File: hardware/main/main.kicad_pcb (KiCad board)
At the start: 4 copper layers, 59.7 x 109.5 mm, 218 parts, among them J101 ST_LINK, J102 USART, J301 Overvoltage_protection, J302 Rad_sensor, J303 Mos_temp, J304 Diode_temp, J601 Supplies, J801 RJ45_Shielded, J802 RJ45_Shielded, Q401 BSC093N15NS5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

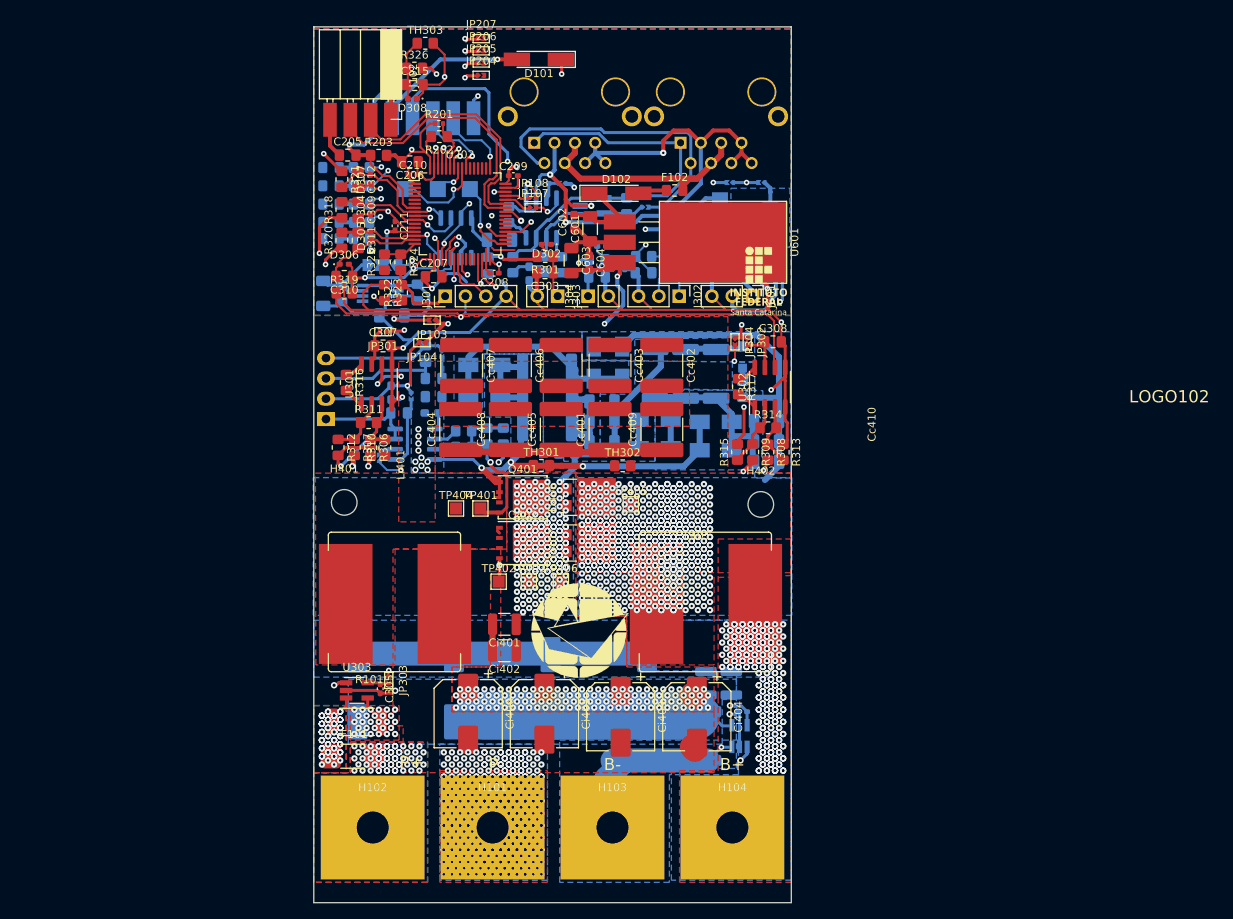
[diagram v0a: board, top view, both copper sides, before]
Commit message: Layout: Designing thermal dissipation and optimizing control
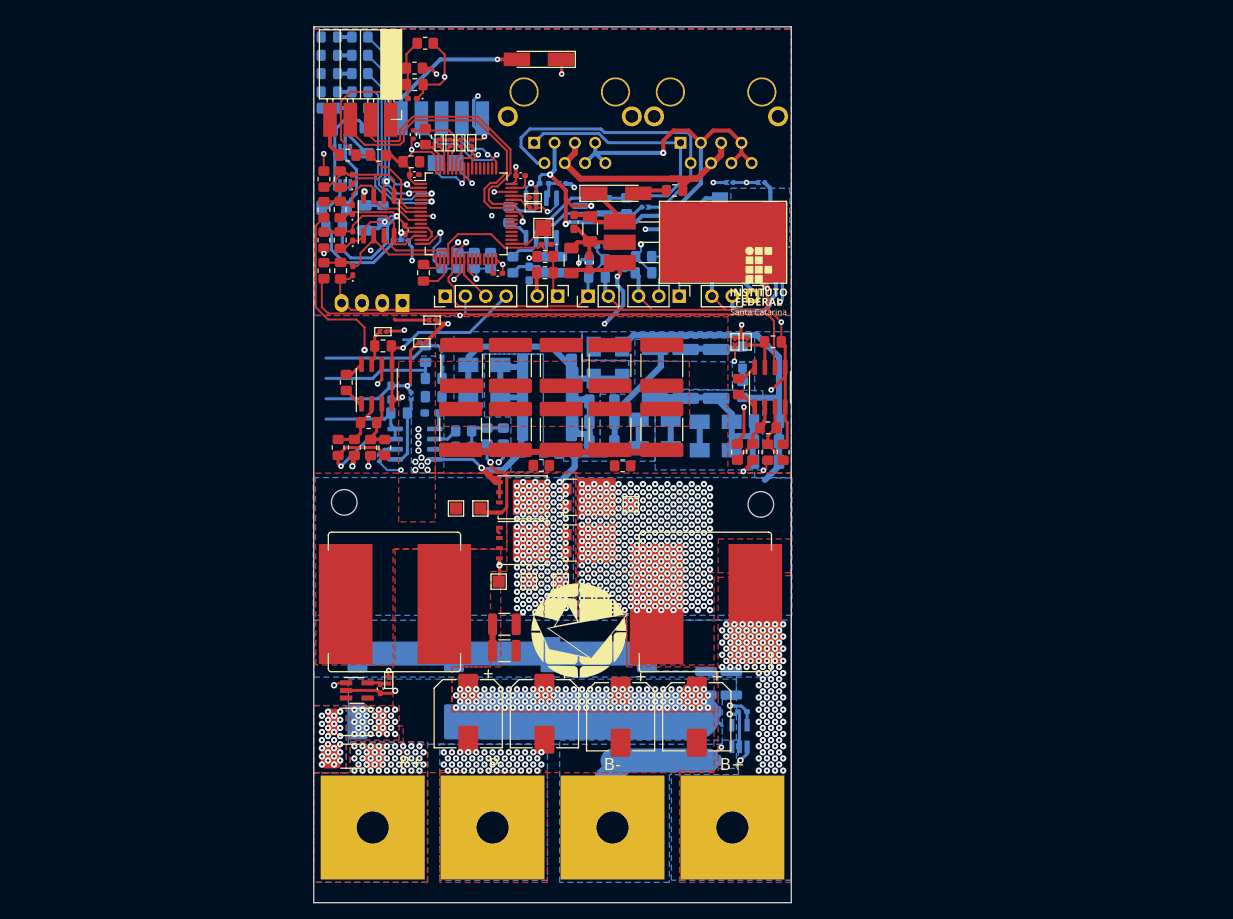
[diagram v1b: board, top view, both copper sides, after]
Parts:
- added HS401: HS10334, Zenite:HS10334 60mmx17mm, B.Cu at (78.7, 156.0)
- D201: value CAN_TX_LED -> CAN_BUSY
- D202: value CAN_RX_LED -> STATUS_LED
- JP203: footprint Jumper:SolderJumper-3_P2.0mm_Open_TrianglePad1.0x1.5mm -> Zenite:SolderJumper-3_P0.5mm_Open_TrianglePad0.8x0.5mm
- R322, R323, R324, R325: moved to B.Cu
- TP203, U305: moved to F.Cu
- moved C202 22.4 mm to (22.3, 95.4), turned to 180 degrees
- moved C201 22.1 mm to (25.4, 96.8), turned to 90 degrees
- moved PS501 17.4 mm to (29.9, 117.1), turned to 90 degrees
- moved C313 17.1 mm to (25.1, 106.4), turned to -90 degrees
- moved U201 16.4 mm to (22.4, 100.1), turned to -90 degrees
- moved D201 16.3 mm to (20.7, 90.7)
- moved D202 16.3 mm to (20.7, 88.4)
- moved D203 16.3 mm to (20.7, 86.1)
- moved D204 16.3 mm to (20.7, 83.8)
- moved D205 16.3 mm to (20.7, 92.7)
- moved R204 16.3 mm to (24.6, 90.7)
- moved R205 16.3 mm to (24.6, 88.4)
- moved R206 16.3 mm to (24.6, 86.1)
- moved R207 16.3 mm to (24.6, 83.8)
- moved R208 16.3 mm to (24.6, 92.7)
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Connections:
- R204 pad 1: Net-(R204-Pad1) -> /STM32/CAN_BUSY
- R205 pad 1: Net-(R205-Pad1) -> /STM32/STATUS_LED
- R206 pad 1: Net-(R206-Pad1) -> /STM32/LED_1
- R207 pad 1: Net-(R207-Pad1) -> /STM32/LED_0
- U202 pad 2: unconnected-(U202-Pad2) -> /STM32/LED_0
- U202 pad 29: Net-(R204-Pad1) -> unconnected-(U202-Pad29)
- U202 pad 3: unconnected-(U202-Pad3) -> /STM32/LED_1
- U202 pad 30: Net-(R205-Pad1) -> unconnected-(U202-Pad30)
- U202 pad 35: Net-(R206-Pad1) -> unconnected-(U202-Pad35)
- U202 pad 36: Net-(R207-Pad1) -> unconnected-(U202-Pad36)
- U202 pad 4: unconnected-(U202-Pad4) -> /STM32/STATUS_LED
- U202 pad 5: unconnected-(U202-Pad5) -> /STM32/CAN_BUSY
- U305 pad 2: /Analog/V_temp_diode -> /Analog/V_bat_adc+
- U305 pad 3: /Analog/V_bat_adc+ -> /Analog/V_temp_mos
- U305 pad 6: /Analog/V_panel_adc+ -> /Analog/V_temp_diode
- U305 pad 7: /Analog/V_temp_mos -> /Analog/V_panel_adc+
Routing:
- net Net-(R321-Pad1): track 27.1 -> 131.8 mm
- net Net-(R207-Pad1): track 34.2 -> 0.00 mm, vias 2 -> 0
- net Net-(R206-Pad1): track 27.2 -> 0.00 mm, vias 2 -> 0
- net Net-(R205-Pad1): track 26.4 -> 0.00 mm, vias 2 -> 0
- net /Cuk/S: track 84.8 -> 58.7 mm, vias 13 -> 11
- net /STM32/STATUS_LED: track 0.00 -> 24.0 mm, vias 0 -> 1
- net /STM32/LED_0: track 0.00 -> 23.1 mm, vias 0 -> 1
- net Net-(R204-Pad1): track 23.1 -> 0.00 mm, vias 2 -> 0
- net /STM32/CAN_BUSY: track 0.00 -> 22.4 mm, vias 0 -> 1
- net /STM32/LED_1: track 0.00 -> 22.4 mm, vias 0 -> 1
- net Net-(JP207-Pad1): track 21.6 -> 2.94 mm, vias 2 -> 0
- net Net-(JP206-Pad1): track 17.4 -> 2.83 mm, vias 2 -> 0
- net GND: track 524.5 -> 539.0 mm, vias 19 -> 20
- net /Analog/Vbat_comp_EXT: track 19.1 -> 5.92 mm, vias 2 -> 1
- net Net-(JP205-Pad1): track 15.3 -> 2.98 mm, vias 2 -> 0
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
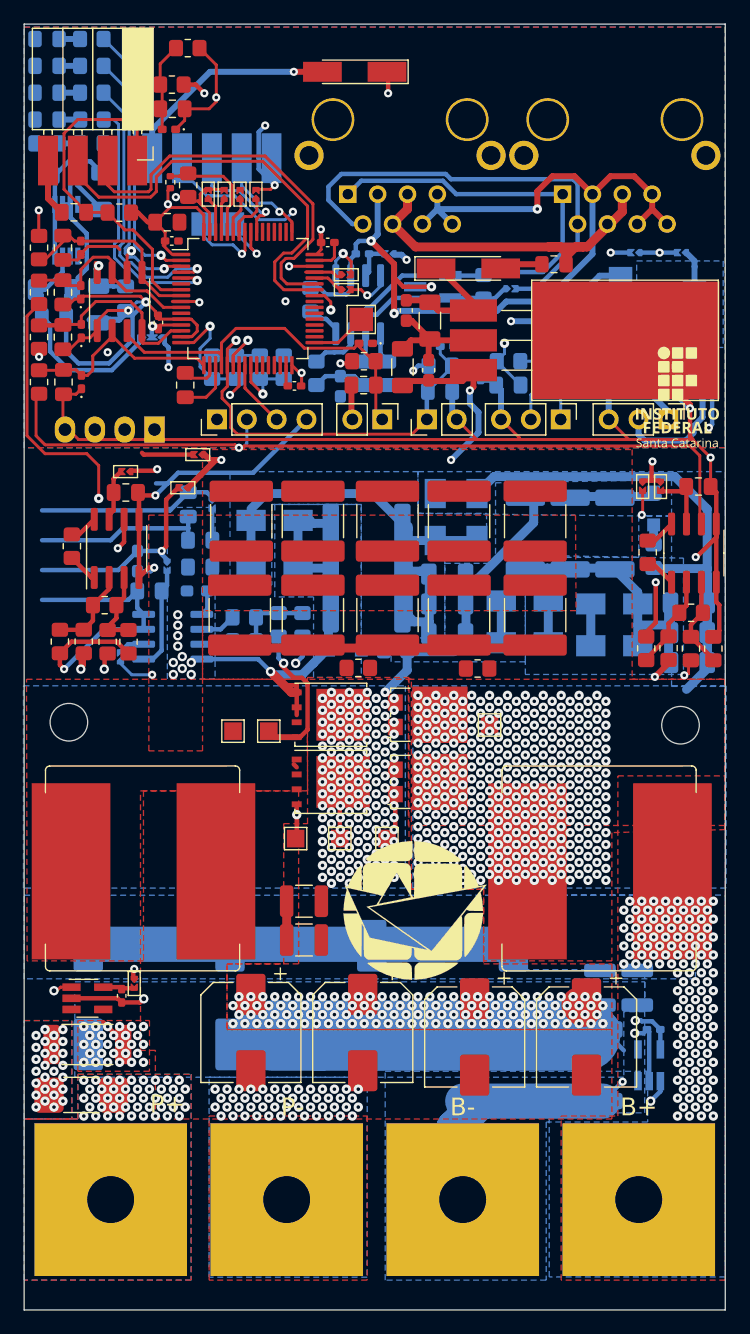
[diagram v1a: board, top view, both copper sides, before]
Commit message: Layout: Connect all unconected nets, and fix all DRC errors
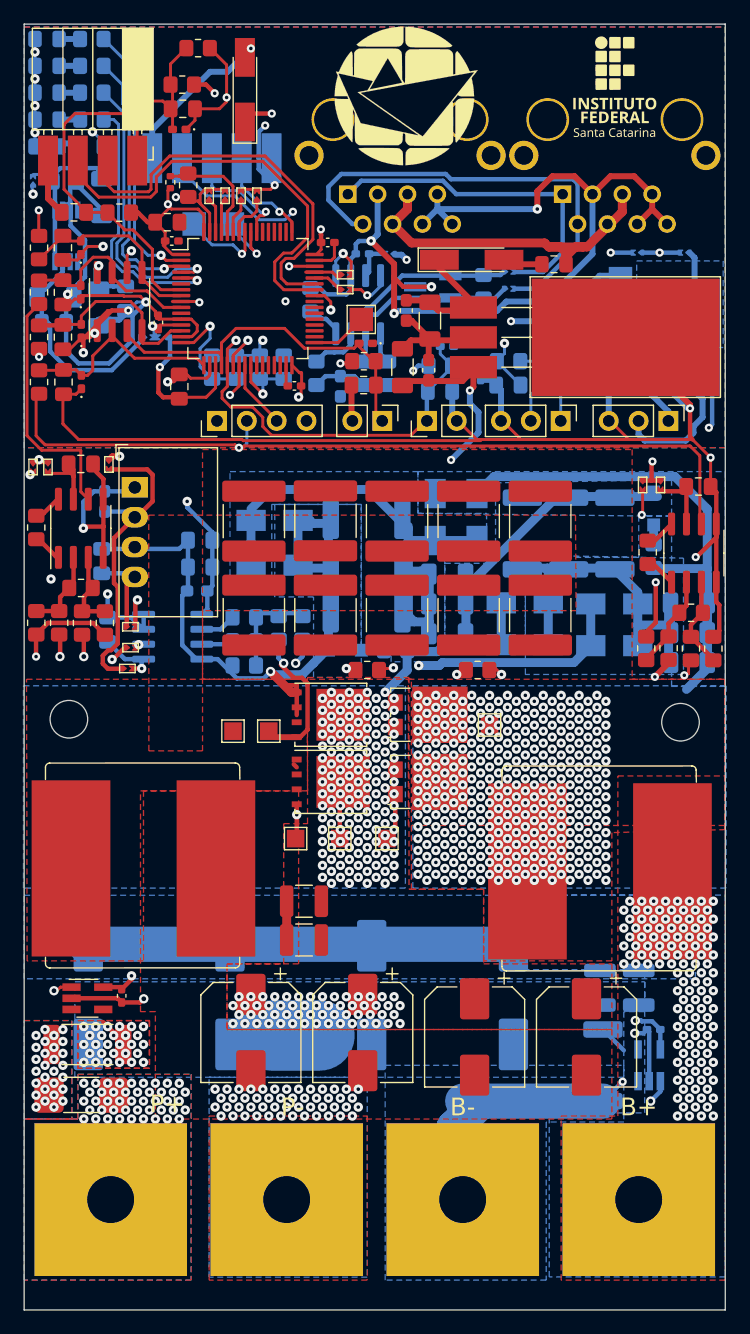
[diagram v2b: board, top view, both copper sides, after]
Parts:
- added R401: 10kR 0805, Resistor_SMD:R_0805_2012Metric_Pad1.20x1.40mm_HandSolder, B.Cu at (37.5, 137.2)
- JP101, JP102, JP104, JP105, JP107, JP108, JP109, JP110, JP201, JP204, JP205, JP206, JP207, JP301, JP302, JP303, JP304: footprint Zenite:SolderJumper-2_P0.5mm_Open_TrianglePad0.5x0.5mm -> Zenite:SolderJumper-2_P0.5mm_Open_TrianglePad0.8x0.5mm
- JP103: footprint Zenite:SolderJumper-2_P0.5mm_Open_TrianglePad0.5x0.5mm -> Zenite:SolderJumper-2_P0.5mm_Open_TrianglePad0.8x0.5mm; moved to B.Cu
- JP106, JP501, JP502: footprint Zenite:SolderJumper-2_P0.5mm_Open_TrianglePad0.5x0.5mm -> Zenite:SolderJumper-2_P0.5mm_Open_TrianglePad0.8x0.5mm; moved to F.Cu
- PS501: moved to F.Cu
- moved LOGO101 69.3 mm to (51.3, 88.6)
- moved JP303 44.2 mm to (19.6, 120.9)
- moved JP103 27.7 mm to (19.6, 95.3), turned to 90 degrees
- moved LOGO102 26.9 mm to (69.1, 87.9)
- moved JP501 12.2 mm to (28.4, 133.9), turned to 0 degrees
- moved D101 9.47 mm to (37.6, 88.1), turned to 90 degrees
- moved JP502 9.12 mm to (28.2, 137.4), turned to 0 degrees
- moved C502 8.81 mm to (25.4, 128.3), turned to 90 degrees
- moved JP301 6.61 mm to (20.8, 120.9), turned to -90 degrees
- moved JP104 6.45 mm to (26.0, 120.7), turned to -90 degrees
- moved C501 5.80 mm to (25.7, 123.2), turned to -90 degrees
- moved PS501 5.20 mm to (28.2, 122.0), turned to 0 degrees
- moved C503 4.85 mm to (25.9, 134.1), turned to 90 degrees
- moved C307 4.54 mm to (23.6, 120.0)
- moved U301 3.50 mm to (23.6, 125.5)
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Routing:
- net GND: track 539.0 -> 609.3 mm, vias 20 -> 32
- net /Analog/3V3_IPanel: track 2.73 -> 51.2 mm, vias 0 -> 2
- net +5V: track 86.7 -> 124.2 mm, vias 5 -> 6
- net /Cuk/S: track 58.7 -> 91.6 mm, vias 11 -> 2
- net /Cuk/A: track 84.4 -> 54.2 mm, vias 302 -> 234
- net /Cuk/C: track 76.0 -> 50.6 mm
- net /3V3_Analog: track 182.8 -> 160.3 mm
- net /Analog/V_temp_diode: track 51.2 -> 73.6 mm, vias 2 -> 3
- net /STM32/Bat_OverV_Out: track 16.6 -> 37.7 mm
- net /Analog/V_temp_mos: track 32.9 -> 53.0 mm, vias 0 -> 1
- net /Cuk/driver/+15V_isolated: track 9.34 -> 24.0 mm, vias 0 -> 2
- net /STM32/3V3_MCU: track 92.6 -> 106.3 mm
- net /3V3_STM: track 34.2 -> 44.5 mm
- net Net-(C502-Pad1): track 15.4 -> 6.06 mm
- net Net-(R318-Pad1): track 29.2 -> 21.1 mm, vias 2 -> 0
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- added copper zone on In1.Cu, net /B+
- added copper zone on In2.Cu, net /B+
- added copper zone on In1.Cu, net /Cuk/A
- added copper zone on In2.Cu, net /Cuk/A
- added copper zone on In1.Cu, net /Cuk/C
- added copper zone on In2.Cu, net /Cuk/C
- added copper zone on In1.Cu, net /P+
- added copper zone on In2.Cu, net /P+
- added copper zone on In1.Cu, net GND
- added copper zone on In2.Cu, net GND

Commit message: Layout: Create Copper zone under NTC temperature sensor for a better thermal coupling
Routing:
- net GND: track 609.3 -> 608.7 mm
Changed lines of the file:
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@@
   (segment (start 54.9656 108.3056) (end 55.621 108.961) (width 0.508) (layer "In1.Cu") (net 1))
   (segment (start 54.727 117.055) (end 54.771 117.055) (width 0.254) (layer "In2.Cu") (net 1))
-  (segment (start 48.702 118.806) (end 48.702 135.956) (width 0.254) (layer "In2.Cu") (net 1))
+  (segment (start 46.741 116.845) (end 48.702 118.806) (width 0.254) (layer "In2.Cu") (net 1))
   (segment (start 58.201 136.687) (end 55.287052 136.687) (width 0.254) (layer "In2.Cu") (net 1))
   (segment (start 53.535 134.934948) (end 53.535 118.247) (width 0.254) (layer "In2.Cu") (net 1))
-  (segment (start 47.244 137.414) (end 46.228 137.414) (width 0.254) (layer "In2.Cu") (net 1))
+  (segment (start 48.702 118.806) (end 48.702 134.432) (width 0.254) (layer "In2.Cu") (net 1))
+  (segment (start 46.228 136.906) (end 46.228 137.414) (width 0.254) (layer "In2.Cu") (net 1))
   (segment (start 53.535 118.247) (end 54.727 117.055) (width 0.254) (layer "In2.Cu") (net 1))
-  (segment (start 48.702 135.956) (end 47.244 137.414) (width 0.254) (layer "In2.Cu") (net 1))
   (segment (start 19.812 135.412144) (end 21.082 134.142144) (width 0.381) (layer "In2.Cu") (net 1))
   (segment (start 19.812 136.398) (end 19.812 135.412144) (width 0.381) (layer "In2.Cu") (net 1))
+  (segment (start 48.702 134.432) (end 46.228 136.906) (width 0.254) (layer "In2.Cu") (net 1))
   (segment (start 59.436 137.922) (end 58.201 136.687) (width 0.254) (layer "In2.Cu") (net 1))
   (segment (start 21.082 134.142144) (end 21.082 129.794) (width 0.381) (layer "In2.Cu") (net 1))
   (segment (start 54.771 117.055) (end 55.621 116.205) (width 0.254) (layer "In2.Cu") (net 1))
   (segment (start 55.287052 136.687) (end 53.535 134.934948) (width 0.254) (layer "In2.Cu") (net 1))
-  (segment (start 46.741 116.845) (end 48.702 118.806) (width 0.254) (layer "In2.Cu") (net 1))
   (segment (start 70.778373 168.464498) (end 71.506002 168.464498) (width 0.381) (layer "B.Cu") (net 1))
   (segment (start 22.3735 107.442) (end 22.3735 105.681) (width 0.381) (layer "B.Cu") (net 1))
@@
   (segment (start 49.006 137.414) (end 50.175362 137.414) (width 0.254) (layer "F.Cu") (net 9))
   (via (at 50.233681 137.355681) (size 0.8) (drill 0.3) (layers "F.Cu" "B.Cu") (remove_unused_layers) (net 9))
-  (segment (start 49.281 136.403) (end 50.233681 137.355681) (width 0.25) (layer "In2.Cu") (net 9))
-  (segment (start 49.281 116.205) (end 49.281 136.403) (width 0.25) (layer "In2.Cu") (net 9))
+  (segment (start 49.281 134.879) (end 50.233681 135.831681) (width 0.25) (layer "In2.Cu") (net 9))
+  (segment (start 50.233681 135.831681) (end 50.233681 137.355681) (width 0.25) (layer "In2.Cu") (net 9))
+  (segment (start 49.281 116.205) (end 49.281 134.879) (width 0.25) (layer "In2.Cu") (net 9))
   (segment (start 36.596 110.747562) (end 37.846 109.497562) (width 0.254) (layer "F.Cu") (net 10))
   (segment (start 37.846 109.497562) (end 37.846 109.474) (width 0.254) (layer "F.Cu") (net 10))
@@
       )
     )
+  )
+  (zone (net 19) (net_name "/Cuk/C") (layer "In1.Cu") (hatch edge 0.508)
+    (priority 6)
+    (connect_pads yes (clearance 0.508))
+    (min_thickness 0.254) (filled_areas_thickness no)
+    (fill yes (thermal_gap 0.508) (thermal_bridge_width 0.508))
+    (polygon
+      (pts
+        (xy 59.436 139.954)
+        (xy 55.626 139.954)
+        (xy 55.626 136.398)
+        (xy 59.436 136.398)
+      )
+    )
+  )
+  (zone (net 107) (net_name "/Cuk/A") (layer "In1.Cu") (hatch edge 0.508)
+    (priority 6)
+    (connect_pads yes (clearance 0.508))
+    (min_thickness 0.254) (filled_areas_thickness no)
+    (fill yes (thermal_gap 0.508) (thermal_bridge_width 0.508))
+    (polygon
+      (pts
+        (xy 50.038 139.954)
+        (xy 46.228 139.954)
+        (xy 46.228 136.398)
+        (xy 50.038 136.398)
+      )
+    )
